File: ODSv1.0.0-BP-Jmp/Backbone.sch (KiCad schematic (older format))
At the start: 32 parts, among them J1 Conn_01x16

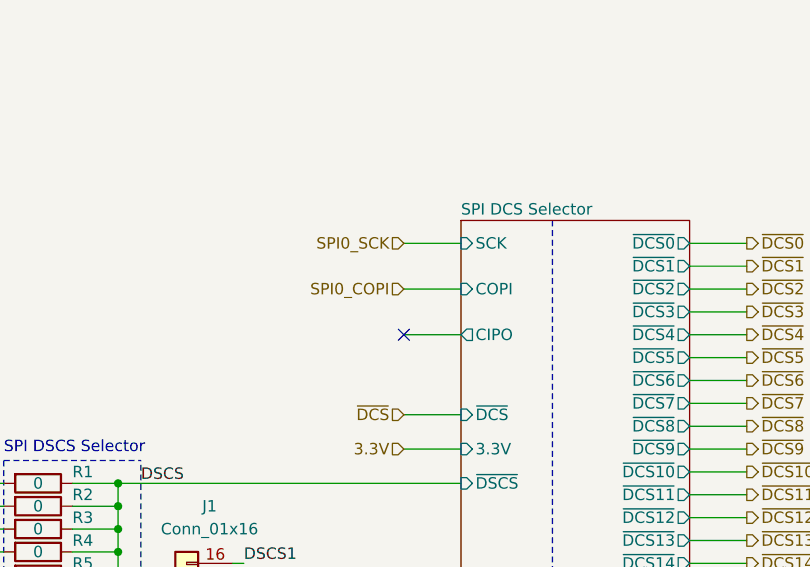
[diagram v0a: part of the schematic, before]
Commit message: Insert 3-state buffers between all MAX7317 DOUTs and CIPO (#16)
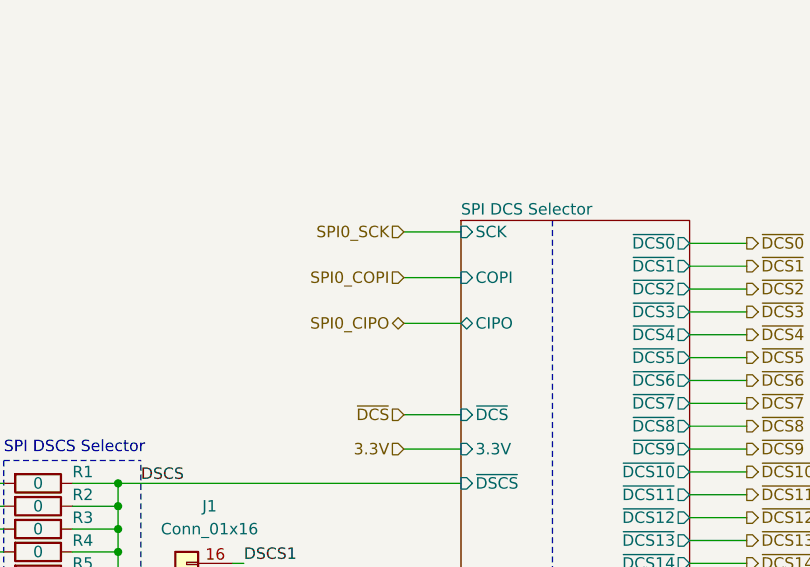
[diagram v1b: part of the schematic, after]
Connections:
- no-connect marks 1 -> 0
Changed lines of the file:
@@
 Text HLabel 5750 3750 0    50   Input ~ 0
 3.3V
-Text HLabel 5750 3050 0    50   Input ~ 0
+Text HLabel 5750 3000 0    50   Input ~ 0
 SPI0_COPI
-Text HLabel 5750 2850 0    50   Input ~ 0
+Text HLabel 5750 2800 0    50   Input ~ 0
 SPI0_SCK
 Wire Wire Line
 	5750 3750 6000 3750
 Wire Wire Line
-	5750 3250 6000 3250
-Wire Wire Line
-	5750 3050 6000 3050
-Wire Wire Line
-	6000 2850 5750 2850
+	5750 3200 6000 3200
+Wire Wire Line
+	5750 3000 6000 3000
+Wire Wire Line
+	6000 2800 5750 2800
 Text HLabel 3500 2800 2    50   Output ~ 0
 SPI0_SCK
@@
 Wire Wire Line
 	5750 3600 6000 3600
-NoConn ~ 5750 3250
 $Sheet
 S 6000 2750 1000 2300
@@
 F0 "SPI DCS Selector" 50
 F1 "SPIDCSSelector.sch" 50
-F2 "SCK" I L 6000 2850 50
-F3 "COPI" I L 6000 3050 50
-F4 "CIPO" O L 6000 3250 50
+F2 "SCK" I L 6000 2800 50
+F3 "COPI" I L 6000 3000 50
+F4 "CIPO" T L 6000 3200 50
 F5 "~DSCS~" I L 6000 3900 50
 F6 "3.3V" I L 6000 3750 50
@@
 F28 "~DCS15~" O R 7000 4350 50
 $EndSheet
+Text HLabel 5750 3200 0    50   3State ~ 0
+SPI0_CIPO
 $EndSCHEMATC

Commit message: Add 2k pullups within DCS selectors (#17), bump BP-Jmp to 0.2.0
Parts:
- J3: renamed from J1; Config (none) -> -NoIC
- R24: renamed from R19; Digikey ID 311-2.00KHRCT-ND -> 311-20.0KHRCT-ND; MPN RC0603FR-072KL -> RC0603FR-0720KL; Ordering URL https://www.digikey.com/en/products/detail/yageo/RC0603FR-072KL/727009 -> https://www.digikey.com/en/products/detail/yageo/RC0603FR-0720KL/727040
- R25: renamed from R20; Digikey ID 311-2.00KHRCT-ND -> 311-20.0KHRCT-ND; MPN RC0603FR-072KL -> RC0603FR-0720KL; Ordering URL https://www.digikey.com/en/products/detail/yageo/RC0603FR-072KL/727009 -> https://www.digikey.com/en/products/detail/yageo/RC0603FR-0720KL/727040
- R26: renamed from R21; Digikey ID 311-2.00KHRCT-ND -> 311-20.0KHRCT-ND; MPN RC0603FR-072KL -> RC0603FR-0720KL; Ordering URL https://www.digikey.com/en/products/detail/yageo/RC0603FR-072KL/727009 -> https://www.digikey.com/en/products/detail/yageo/RC0603FR-0720KL/727040
- R27: renamed from R22; Digikey ID 311-2.00KHRCT-ND -> 311-20.0KHRCT-ND; MPN RC0603FR-072KL -> RC0603FR-0720KL; Ordering URL https://www.digikey.com/en/products/detail/yageo/RC0603FR-072KL/727009 -> https://www.digikey.com/en/products/detail/yageo/RC0603FR-0720KL/727040
- R28: renamed from R23; Digikey ID 311-2.00KHRCT-ND -> 311-20.0KHRCT-ND; MPN RC0603FR-072KL -> RC0603FR-0720KL; Ordering URL https://www.digikey.com/en/products/detail/yageo/RC0603FR-072KL/727009 -> https://www.digikey.com/en/products/detail/yageo/RC0603FR-0720KL/727040
- renumbered R16 to R21, R17 to R22, R18 to R23
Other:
- moved on the sheet: D1, D2, D3, J3, R21, R22, R23
